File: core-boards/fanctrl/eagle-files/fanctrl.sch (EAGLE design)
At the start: 30 parts, among them J1 3-PIN_2MM-H, U1 MCP9701T-E/TT

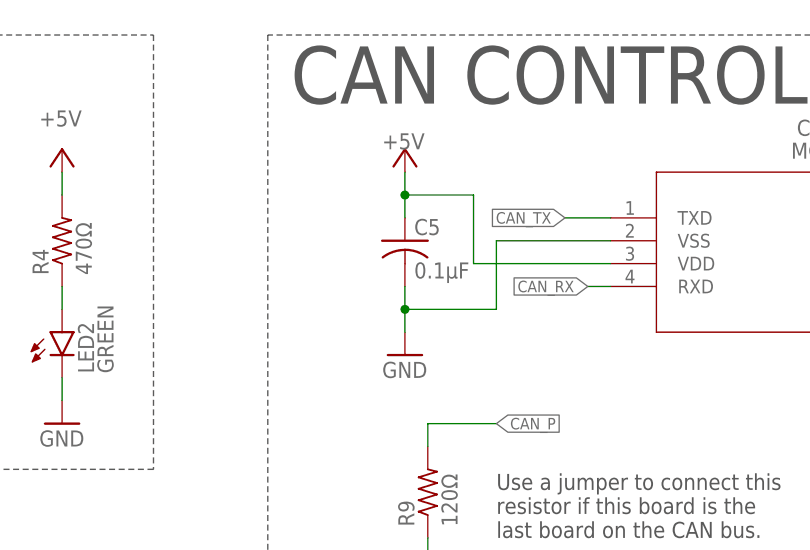
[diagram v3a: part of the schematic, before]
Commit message: Add 3A fuse to +5V from CAN bus.
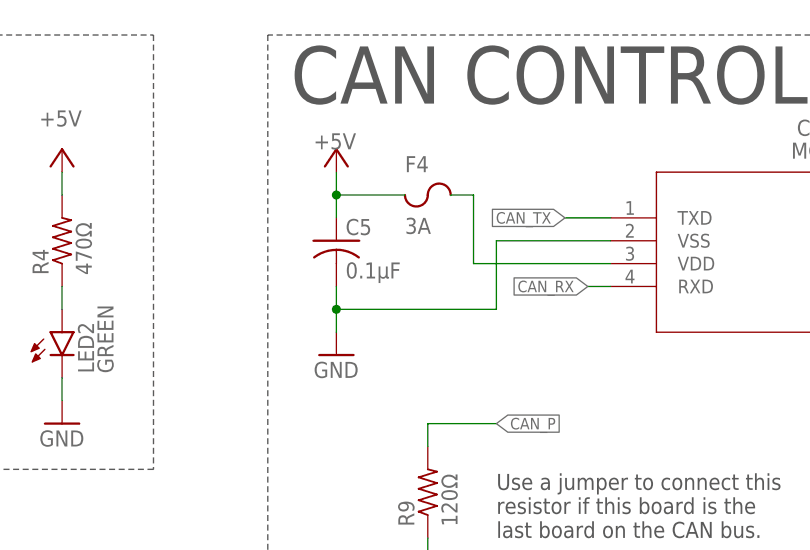
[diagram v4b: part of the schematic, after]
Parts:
- added F4: 3A, RoboJackets-Fuses:CHIP_FUSE1206
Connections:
- new net N$6: CAN-CONTROLLER.VDD, F4.2
- net +5V: now also F4.1; no longer CAN-CONTROLLER.VDD
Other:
- moved on the sheet: C5
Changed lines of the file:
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@@
 <attribute name="SPICEPREFIX" value="B"/>
 </part>
+<part name="F4" library="RoboJackets-Fuses" deviceset="CHIP_FUSE" device="1206" value="3A"/>
 </parts>
 <sheets>
@@
 <attribute name="VALUE" x="213.0806" y="194.5386" size="1.778" layer="96" rot="SR0"/>
 </instance>
-<instance part="C5" gate="G$1" x="170.18" y="185.42" smashed="yes">
-<attribute name="NAME" x="171.196" y="186.055" size="1.778" layer="95"/>
-<attribute name="VALUE" x="171.196" y="181.229" size="1.778" layer="96"/>
-</instance>
-<instance part="GND12" gate="1" x="170.18" y="172.72" smashed="yes">
-<attribute name="VALUE" x="167.64" y="170.18" size="1.778" layer="96"/>
-</instance>
-<instance part="P+8" gate="1" x="170.18" y="195.58" smashed="yes">
-<attribute name="VALUE" x="167.64" y="195.58" size="1.778" layer="96"/>
+<instance part="C5" gate="G$1" x="162.56" y="185.42" smashed="yes">
+<attribute name="NAME" x="163.576" y="186.055" size="1.778" layer="95"/>
+<attribute name="VALUE" x="163.576" y="181.229" size="1.778" layer="96"/>
+</instance>
+<instance part="GND12" gate="1" x="162.56" y="172.72" smashed="yes">
+<attribute name="VALUE" x="160.02" y="170.18" size="1.778" layer="96"/>
+</instance>
+<instance part="P+8" gate="1" x="162.56" y="195.58" smashed="yes">
+<attribute name="VALUE" x="160.02" y="195.58" size="1.778" layer="96"/>
 </instance>
 <instance part="C6" gate="G$1" x="246.38" y="175.26" smashed="yes">
@@
 <attribute name="NAME" x="161.29" y="147.955" size="1.778" layer="95"/>
 <attribute name="VALUE" x="161.29" y="137.16" size="1.778" layer="96"/>
+</instance>
+<instance part="F4" gate="G$1" x="172.72" y="190.5" smashed="yes">
+<attribute name="NAME" x="170.18" y="193.04" size="1.778" layer="95"/>
+<attribute name="VALUE" x="170.18" y="187.96" size="1.778" layer="96" align="top-left"/>
 </instance>
 </instances>
@@
 <wire x1="193.04" y1="185.42" x2="180.34" y2="185.42" width="0.1524" layer="91"/>
 <wire x1="180.34" y1="185.42" x2="180.34" y2="177.8" width="0.1524" layer="91"/>
-<wire x1="180.34" y1="177.8" x2="170.18" y2="177.8" width="0.1524" layer="91"/>
+<wire x1="180.34" y1="177.8" x2="162.56" y2="177.8" width="0.1524" layer="91"/>
 <pinref part="C5" gate="G$1" pin="2"/>
-<wire x1="170.18" y1="177.8" x2="170.18" y2="180.34" width="0.1524" layer="91"/>
-<wire x1="170.18" y1="177.8" x2="170.18" y2="175.26" width="0.1524" layer="91"/>
-<junction x="170.18" y="177.8"/>
+<wire x1="162.56" y1="177.8" x2="162.56" y2="180.34" width="0.1524" layer="91"/>
+<wire x1="162.56" y1="177.8" x2="162.56" y2="175.26" width="0.1524" layer="91"/>
+<junction x="162.56" y="177.8"/>
 <pinref part="GND12" gate="1" pin="GND"/>
 </segment>
@@
 </segment>
 <segment>
-<pinref part="CAN-CONTROLLER" gate="A" pin="VDD"/>
-<wire x1="193.04" y1="182.88" x2="177.8" y2="182.88" width="0.1524" layer="91"/>
-<wire x1="177.8" y1="182.88" x2="177.8" y2="190.5" width="0.1524" layer="91"/>
-<wire x1="177.8" y1="190.5" x2="170.18" y2="190.5" width="0.1524" layer="91"/>
+<pinref part="P+8" gate="1" pin="+5V"/>
 <pinref part="C5" gate="G$1" pin="1"/>
-<wire x1="170.18" y1="190.5" x2="170.18" y2="187.96" width="0.1524" layer="91"/>
-<wire x1="170.18" y1="190.5" x2="170.18" y2="193.04" width="0.1524" layer="91"/>
-<junction x="170.18" y="190.5"/>
-<pinref part="P+8" gate="1" pin="+5V"/>
+<wire x1="162.56" y1="187.96" x2="162.56" y2="190.5" width="0.1524" layer="91"/>
+<pinref part="F4" gate="G$1" pin="1"/>
+<wire x1="162.56" y1="190.5" x2="162.56" y2="193.04" width="0.1524" layer="91"/>
+<wire x1="170.18" y1="190.5" x2="162.56" y2="190.5" width="0.1524" layer="91"/>
+<junction x="162.56" y="190.5"/>
 </segment>
 <segment>
@@
 </segment>
 </net>
+<net name="N$6" class="0">
+<segment>
+<pinref part="CAN-CONTROLLER" gate="A" pin="VDD"/>
+<wire x1="193.04" y1="182.88" x2="177.8" y2="182.88" width="0.1524" layer="91"/>
+<wire x1="177.8" y1="182.88" x2="177.8" y2="190.5" width="0.1524" layer="91"/>
+<pinref part="F4" gate="G$1" pin="2"/>
+<wire x1="177.8" y1="190.5" x2="175.26" y2="190.5" width="0.1524" layer="91"/>
+</segment>
+</net>

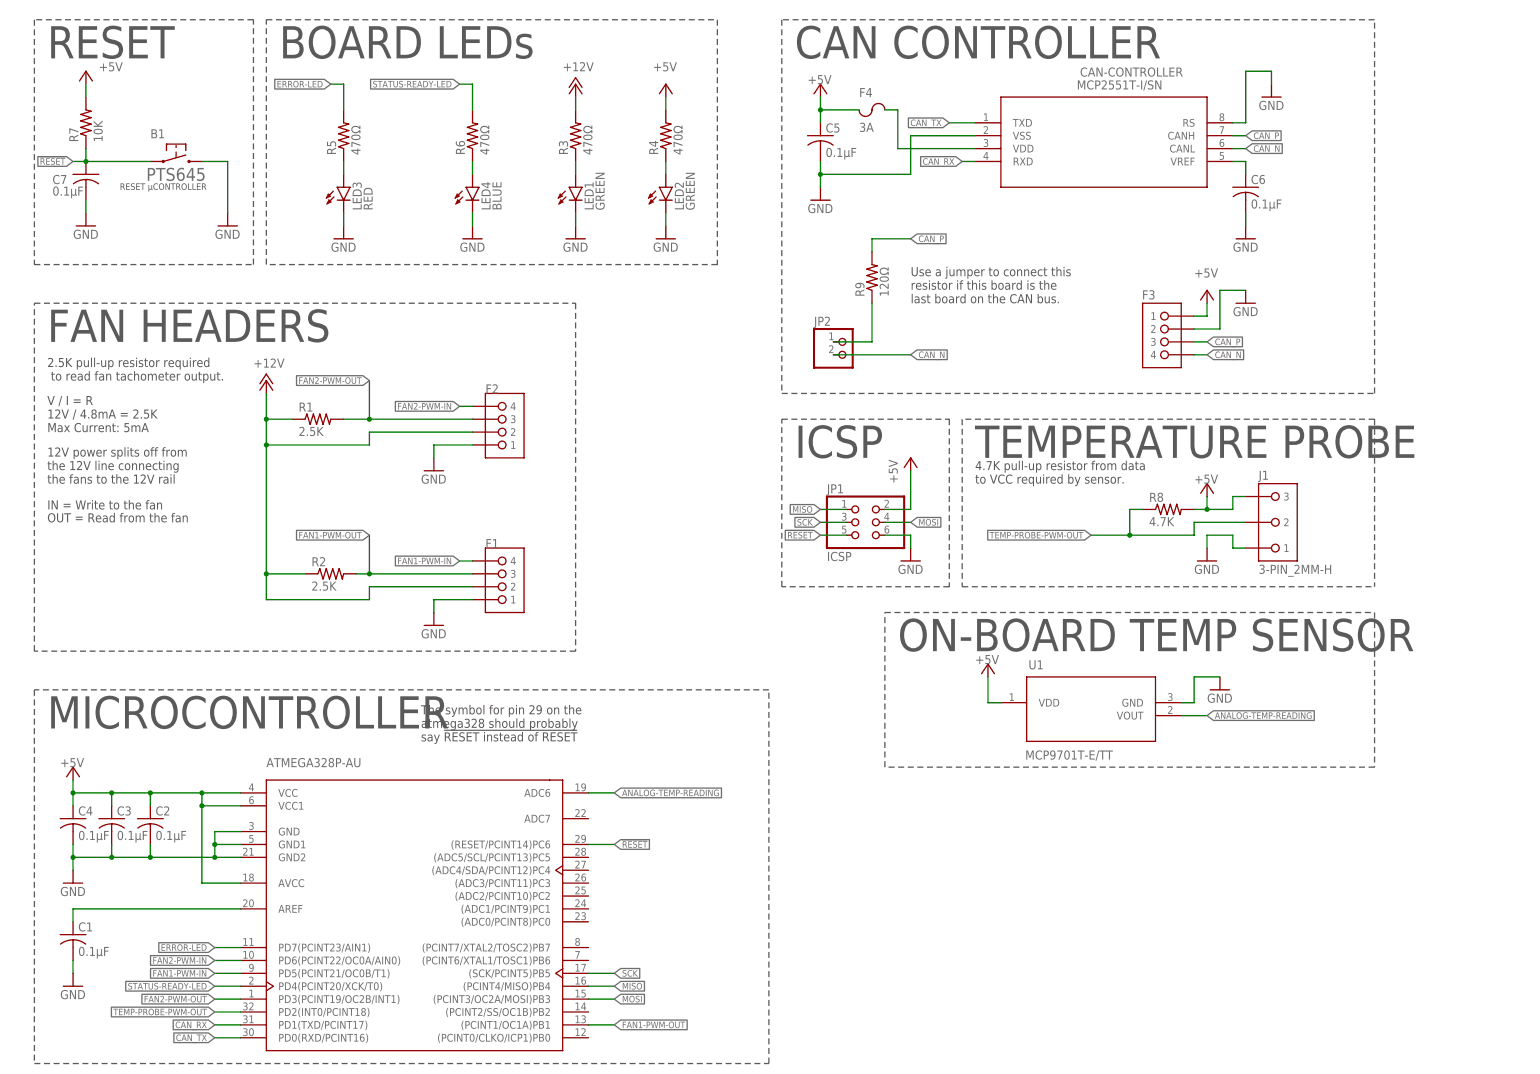
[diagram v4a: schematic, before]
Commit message: Fix LED routing. Fix LED name (ERROR --> INVALID TEMP).
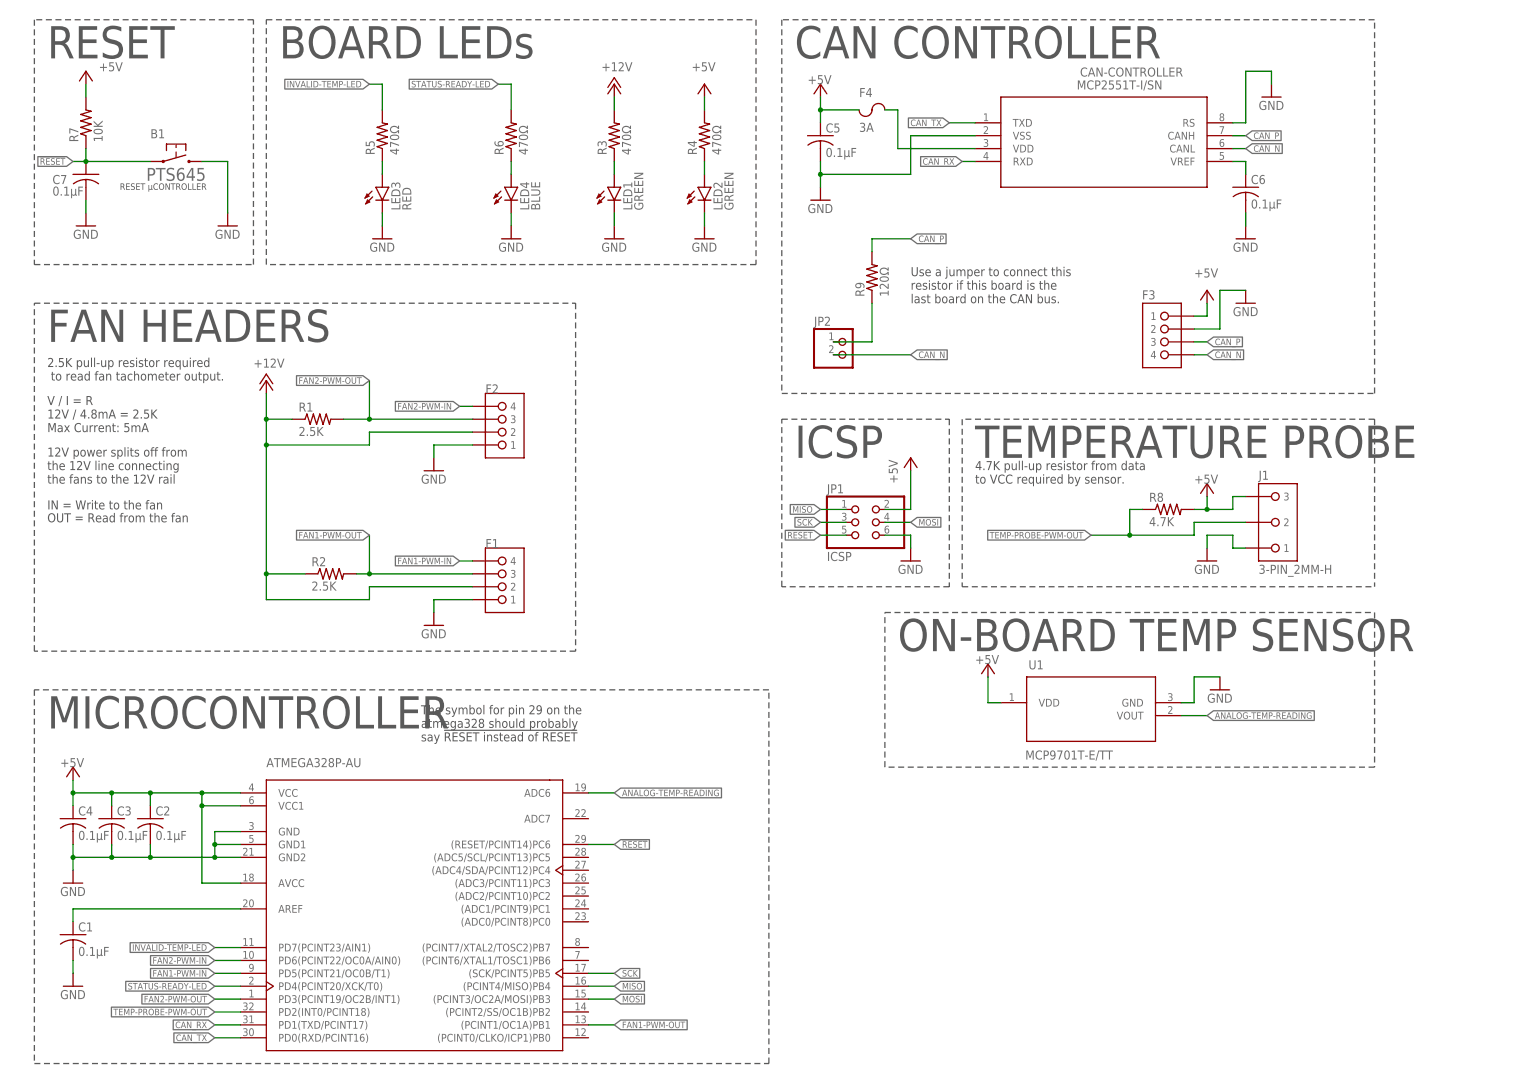
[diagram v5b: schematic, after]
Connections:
- net ERROR-LED renamed INVALID-TEMP-LED
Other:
- moved on the sheet: LED1, LED2, LED3, LED4, R3, R4, R5, R6

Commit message: Fix connector orientation. Change fan signal names for less confusion.
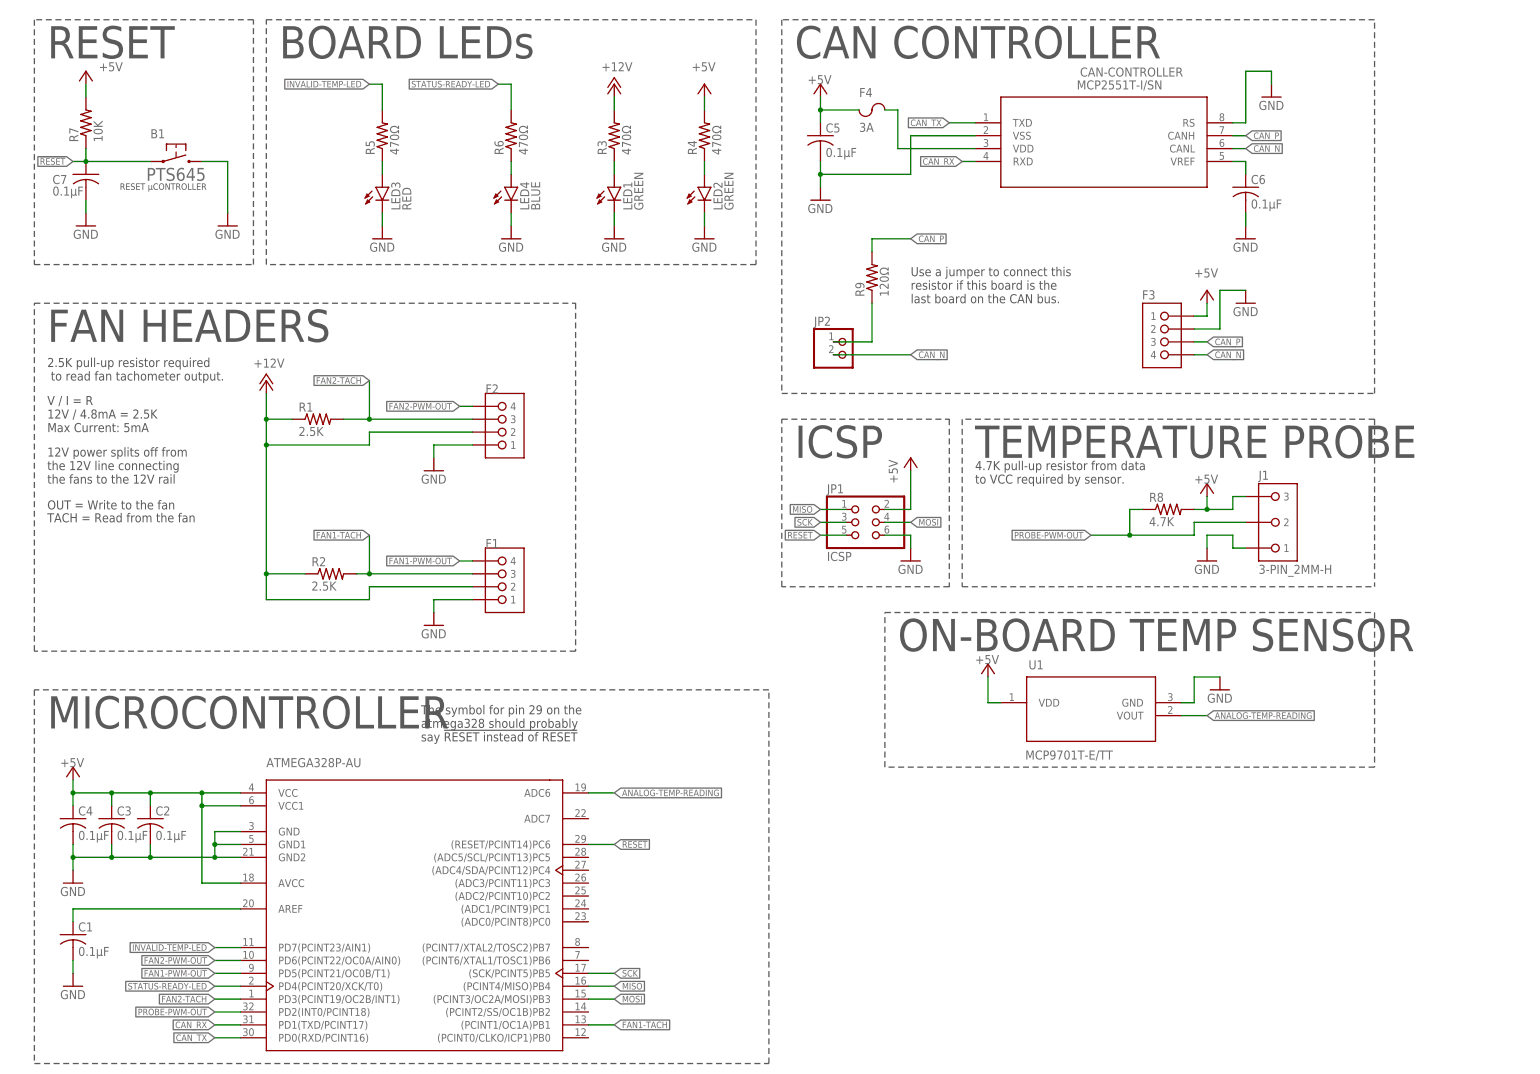
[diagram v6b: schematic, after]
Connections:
- net N$6 renamed +5V_UNFUSED
- net TEMP-PROBE-PWM-OUT renamed PROBE-PWM-OUT
- removed net FAN1-PWM-IN: ATMEGA328.PD5(PCINT21/OC0B/T1), F1.4
- removed net FAN2-PWM-IN: ATMEGA328.PD6(PCINT22/OC0A/AIN0), F2.4
- new net FAN1-TACH: ATMEGA328.(PCINT1/OC1A)PB1, F1.3, R2.2
- new net FAN2-TACH: ATMEGA328.PD3(PCINT19/OC2B/INT1), F2.3, R1.2
- net FAN1-PWM-OUT: now also ATMEGA328.PD5(PCINT21/OC0B/T1), F1.4; no longer ATMEGA328.(PCINT1/OC1A)PB1, F1.3, R2.2
- net FAN2-PWM-OUT: now also ATMEGA328.PD6(PCINT22/OC0A/AIN0), F2.4; no longer ATMEGA328.PD3(PCINT19/OC2B/INT1), F2.3, R1.2
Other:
- note added: "OUT = Write to the fan"
- note added: "TACH = Read from the fan"
- note removed: "IN = Write to the fan"
- note removed: "OUT = Read from the fan"
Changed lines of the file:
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@@
 <wire x1="187.96" y1="96.52" x2="154.94" y2="96.52" width="0.1524" layer="97" style="shortdash"/>
 <text x="157.48" y="121.92" size="6.35" layer="97" font="vector" ratio="12">ICSP</text>
-<text x="10.16" y="111.76" size="1.778" layer="97">IN = Write to the fan</text>
-<text x="10.16" y="109.22" size="1.778" layer="97">OUT = Read from the fan</text>
+<text x="10.16" y="111.76" size="1.778" layer="97">OUT = Write to the fan</text>
+<text x="10.16" y="109.22" size="1.778" layer="97">TACH = Read from the fan</text>
 <text x="180.34" y="152.4" size="1.778" layer="97" font="vector">Use a jumper to connect this
 resistor if this board is the
@@
 </segment>
 </net>
-<net name="FAN2-PWM-OUT" class="0">
+<net name="FAN2-TACH" class="0">
 <segment>
 <pinref part="F2" gate="G$1" pin="3"/>
@@
 </segment>
 </net>
-<net name="FAN1-PWM-OUT" class="0">
+<net name="FAN1-TACH" class="0">
 <segment>
 <pinref part="ATMEGA328" gate="G$1" pin="(PCINT1/OC1A)PB1"/>
@@
 </segment>
 </net>
-<net name="FAN2-PWM-IN" class="0">
+<net name="FAN2-PWM-OUT" class="0">
 <segment>
 <pinref part="ATMEGA328" gate="G$1" pin="PD6(PCINT22/OC0A/AIN0)"/>
@@
 </segment>
 </net>
-<net name="FAN1-PWM-IN" class="0">
+<net name="FAN1-PWM-OUT" class="0">
 <segment>
 <pinref part="ATMEGA328" gate="G$1" pin="PD5(PCINT21/OC0B/T1)"/>
@@
 </segment>
 </net>
-<net name="TEMP-PROBE-PWM-OUT" class="0">
+<net name="PROBE-PWM-OUT" class="0">
 <segment>
 <label x="215.9" y="106.68" size="1.27" layer="95" font="vector" rot="R180" xref="yes"/>
@@
 </segment>
 </net>
-<net name="N$6" class="0">
+<net name="+5V_UNFUSED" class="0">
 <segment>
 <pinref part="CAN-CONTROLLER" gate="A" pin="VDD"/>
